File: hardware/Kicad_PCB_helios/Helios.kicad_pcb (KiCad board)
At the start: 2 copper layers, 75.2 x 61.1 mm, 101 parts, among them P1 USB_B, P2 CONN_01X25-SHIELD, U1 IP4220CZ6, U2 AP2114, U3 AN431B, U4 ISA_DC-DC_converter, U5 DAC084S085C, U6 TL084_v, U7 LM358, U8 TL084_v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

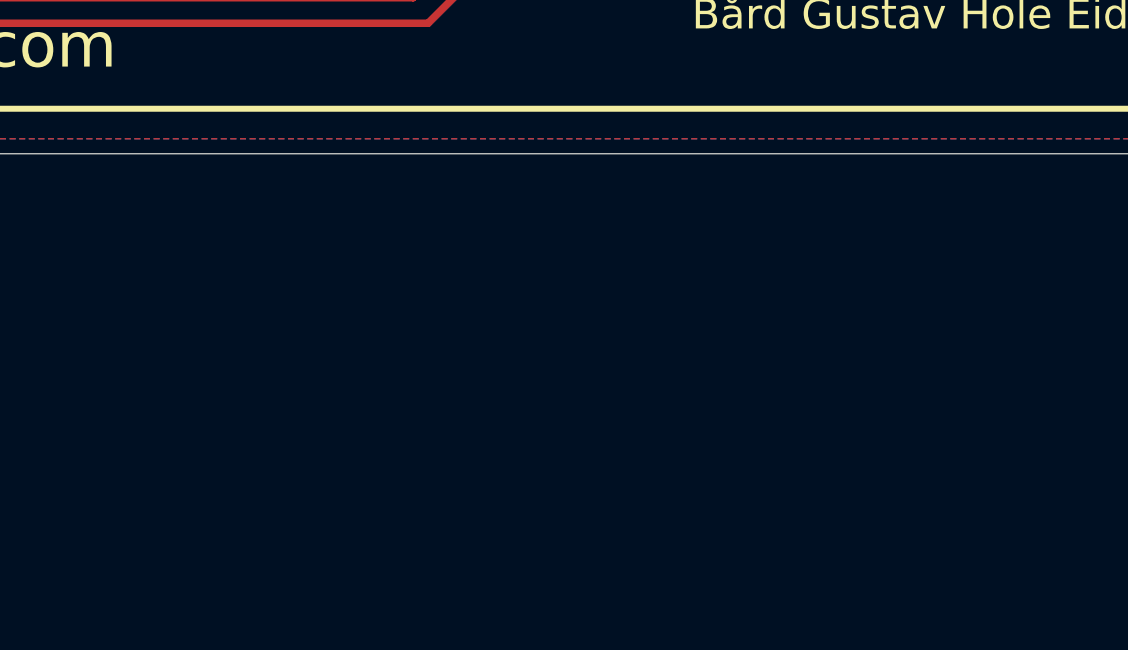
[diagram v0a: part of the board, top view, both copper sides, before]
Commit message: Dodano 2 zewnętrzne 16 bitowe układy DAC
Podłączono VREF do wewnętrznych DAC

Wszystko działa na jednej magistrali SPI
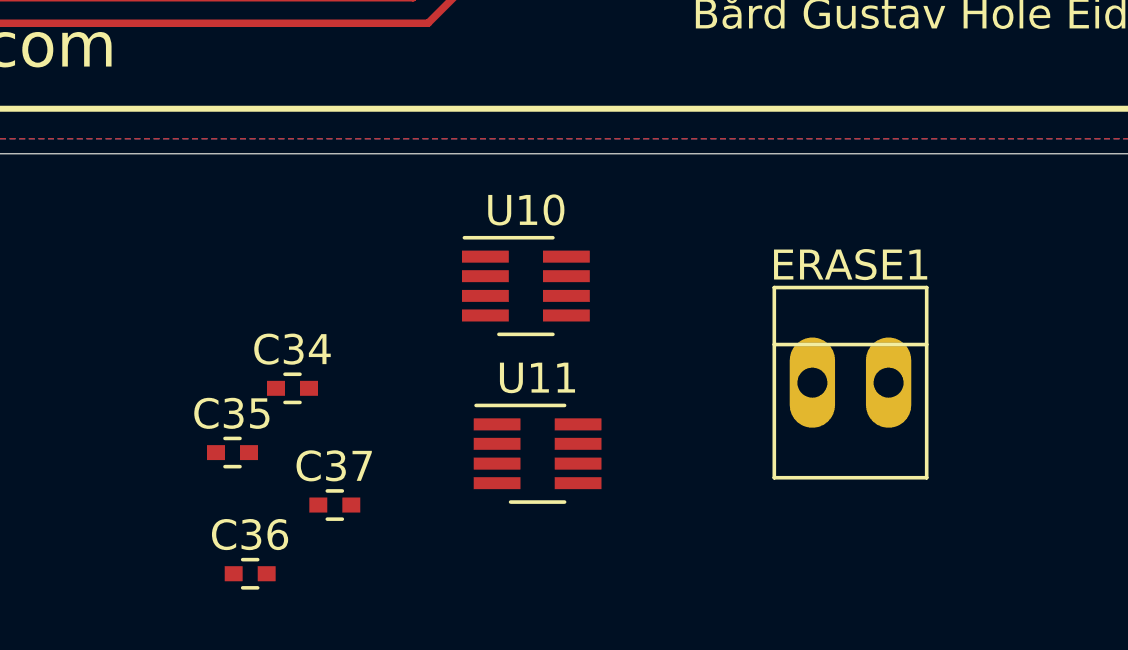
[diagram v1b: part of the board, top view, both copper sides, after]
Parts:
- added C34: 100nF, Capacitors_SMD:C_0402, F.Cu at (129.4, 168.9)
- added C35: 100nF, Capacitors_SMD:C_0402, F.Cu at (127.4, 171.1)
- added C36: 10nF, Capacitors_SMD:C_0402, F.Cu at (128.0, 175.1)
- added C37: 10nF, Capacitors_SMD:C_0402, F.Cu at (130.8, 172.8)
- added ERASE1: CONN_01X02, Connect:PINHEAD1-2, F.Cu at (146.8, 168.7)
- added U10: DAC8531, TO_SOT_Packages_SMD:SOT-23-8_Handsoldering, F.Cu at (137.2, 165.5)
- added U11: DAC8531, TO_SOT_Packages_SMD:SOT-23-8_Handsoldering, F.Cu at (137.6, 171.1)
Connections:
- net /Amplifiers/+9V renamed /+9V
- net /Amplifiers/+B renamed /+B
- net /Amplifiers/+G renamed /+G
- net /Amplifiers/+Intensity renamed /+Int
- net /Amplifiers/+R renamed /+R
- net /Amplifiers/+X renamed /+X
- net /Amplifiers/+Y renamed /+Y
- net /Amplifiers/-9V renamed /-9V
- net /Amplifiers/-X renamed /-X
- net /Amplifiers/-Y renamed /-Y
- net /Amplifiers/2.5V renamed /2.5V
- net /Amplifiers/B renamed /B
- net /Amplifiers/G renamed /G
- net /Amplifiers/Intensity renamed /Int
- net /Amplifiers/R renamed /R
- net /Amplifiers/Shutter renamed /Shutter
- net /Amplifiers/Shutter_Out renamed /Shutter_Out
- net /DAC/!SYNC renamed /DAC/!SYNC-Quad
- net /Power Regulation/5V renamed /VCC
- C10 pad 1: /DAC/3.3V -> /3.3V
- C11 pad 1: /DAC/3.3V -> /3.3V
- C21 pad 1: /DAC/3.3V -> /3.3V
- C23 pad 1: /DAC/3.3V -> /3.3V
- C25 pad 1: /DAC/3.3V -> /3.3V
- C26 pad 1: /DAC/3.3V -> /3.3V
- C27 pad 1: /DAC/3.3V -> /3.3V
- ERASE pad 2: /DAC/3.3V -> (no net)
- F1 pad 1: Net-(F1-Pad1) -> Net-(C2-Pad1)
- P1 pad 1: Net-(F1-Pad1) -> Net-(C2-Pad1)
- P1 pad 5: Net-(C2-Pad1) -> GND
- R12 pad 1: /DAC/3.3V -> /3.3V
- R13 pad 1: /DAC/3.3V -> /3.3V
- R33 pad 1: Net-(R33-Pad1) -> (no net)
- R34 pad 1: Net-(R34-Pad1) -> (no net)
- U2 pad 2: /DAC/3.3V -> /3.3V
- U5 pad 1: /DAC/3.3V -> /3.3V
- U8 pad 10: Net-(R34-Pad1) -> /Amplifiers/Offset
- U8 pad 3: Net-(R33-Pad1) -> /Amplifiers/Offset
- U9 pad 18: /DAC/3.3V -> /3.3V
- U9 pad 29: (no net) -> /DAC/!SYNC-X
- U9 pad 30: (no net) -> /DAC/!SYNC-Y
- U9 pad 45: /DAC/3.3V -> /3.3V
- U9 pad 58: /DAC/3.3V -> /3.3V
- U9 pad 59: /Amplifiers/X -> /DAC/X_SCALING
- U9 pad 63: /Amplifiers/Y -> /DAC/Y_SCALING
- U9 pad 7: /DAC/3.3V -> /3.3V
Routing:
- net /DAC/3.3V: track 95.3 -> 0.00 mm, vias 2 -> 0
- net /3.3V: track 0.00 -> 95.3 mm, vias 0 -> 2
- net /DAC/Y_SCALING: track 0.00 -> 21.6 mm, vias 0 -> 2
- net /Amplifiers/Y: track 45.6 -> 24.0 mm, vias 4 -> 2
- net Net-(F1-Pad1): track 17.2 -> 0.00 mm
- net GND: track 138.7 -> 151.8 mm
- net /DAC/X_SCALING: track 0.00 -> 12.7 mm, vias 0 -> 1
- net /Amplifiers/X: track 44.5 -> 31.8 mm, vias 2 -> 1
- net /Amplifiers/Offset: track 17.3 -> 28.3 mm
- net Net-(R34-Pad1): track 6.09 -> 0.00 mm
- net Net-(R33-Pad1): track 4.89 -> 0.00 mm
- net Net-(C2-Pad1): track 15.5 -> 19.6 mm

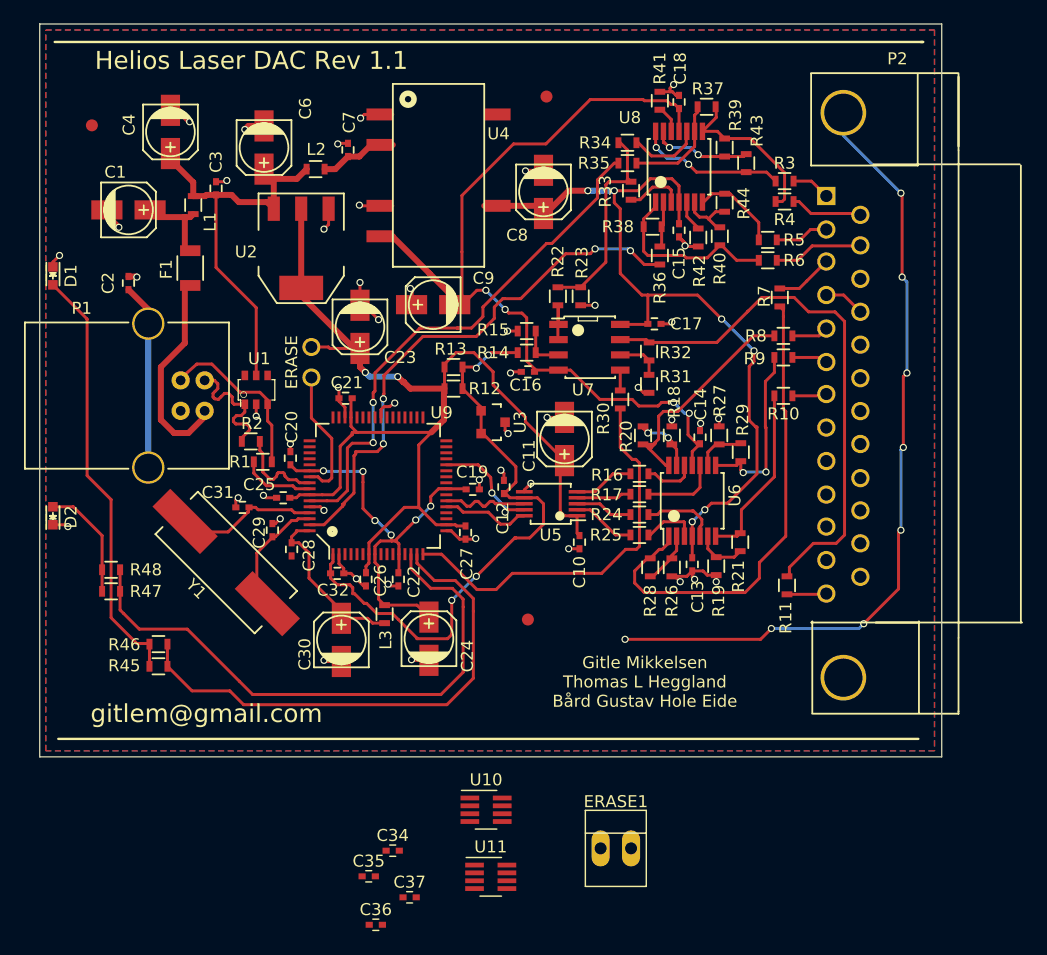
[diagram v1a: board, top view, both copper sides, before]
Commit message: Updated PCB Layout
Changed connector to IDC
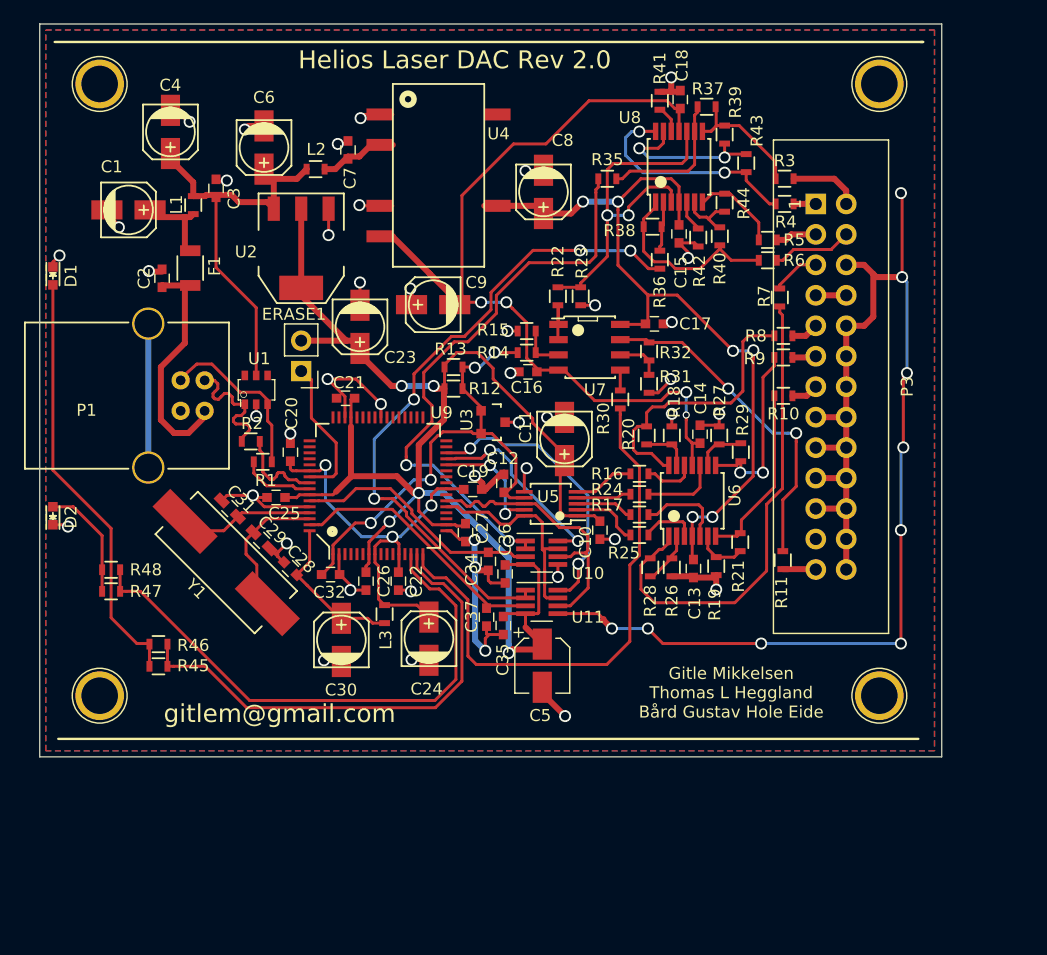
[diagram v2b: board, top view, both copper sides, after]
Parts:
- removed ERASE: CONN_01X02, Connect:PINHEAD1-2
- removed P2: CONN_01X25-SHIELD, personal:DB25
- removed R33, R34: 1.65k, Resistors_SMD:R_0603
- removed REF** (x3): Fiducial_1mm_Dia_2.54mm_Outer_CopperTop, Fiducials:Fiducial_1mm_Dia_2.54mm_Outer_CopperTop
- added C5: 4.7uF, Capacitors_SMD:CP_Elec_4x5.3, F.Cu at (141.9, 153.5)
- added P3: CONN_02X13, Connectors:IDC_Header_Straight_26pins, F.Cu at (164.7, 115.0)
- added W1: TEST_1P, Connectors:1pin, F.Cu at (105.0, 156.0)
- added W2: TEST_1P, Connectors:1pin, F.Cu at (105.0, 105.0)
- added W3: TEST_1P, Connectors:1pin, F.Cu at (170.0, 156.0)
- added W4: TEST_1P, Connectors:1pin, F.Cu at (170.0, 105.0)
- added W5: TEST_1P, Symbols:WEEE-Logo_14x20mm_SilkScreen, B.Cu at (149.7, 129.9)
- C10, C12, C13, C14, C15, C16, C17, C18, C19, C2, C20, C21, C22, C25, C26, C27, C28, C3, C32, C34, C35, C36, C37, C7: footprint Capacitors_SMD:C_0402 -> Capacitors_SMD:C_0603
- C29, C31: footprint Capacitors_SMD:C_0402 -> Capacitors_SMD:C_0603_HandSoldering
- ERASE1: footprint Connect:PINHEAD1-2 -> Pin_Headers:Pin_Header_Straight_1x02_Pitch2.54mm
- moved ERASE1 47.0 mm to (121.8, 128.9), turned to 180 degrees
- moved C36 31.7 mm to (137.4, 144.8), turned to 270 degrees
- moved C34 24.9 mm to (138.8, 145.8), turned to 270 degrees
- moved C37 24.2 mm to (137.2, 149.4), turned to 270 degrees
- moved C35 23.7 mm to (138.7, 150.2), turned to 270 degrees
- moved U11 23.3 mm to (141.8, 148.2)
- moved U10 21.9 mm to (141.8, 144.1)
- moved C2 2.83 mm to (110.2, 121.2)
- moved R11 2.13 mm to (161.9, 144.7)
- moved R35 2.13 mm to (147.3, 112.9)
- moved C10 1.97 mm to (146.7, 142.2)
- moved R3 1.90 mm to (162.1, 115.0)
- moved R4 1.90 mm to (162.1, 112.9)
- moved C28 1.60 mm to (120.9, 145.4), turned to 135 degrees
- moved C29 1.24 mm to (118.5, 143.1), turned to 315 degrees
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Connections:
- R10 pad 1: Net-(P2-Pad7) -> /X7
- R11 pad 1: Net-(P2-Pad13) -> /X13
- R3 pad 1: Net-(P2-Pad1) -> /X1
- R4 pad 1: Net-(P2-Pad14) -> /X14
- R5 pad 1: Net-(P2-Pad2) -> /X2
- R6 pad 1: Net-(P2-Pad15) -> /X15
- R7 pad 1: Net-(P2-Pad3) -> /X3
- R8 pad 1: Net-(P2-Pad5) -> /X5
- R9 pad 1: Net-(P2-Pad6) -> /X6
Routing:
- net GND: track 151.8 -> 234.1 mm, vias 55 -> 53
- net /3.3V: track 95.3 -> 129.7 mm, vias 2 -> 5
- net /Amplifiers/Y: track 24.0 -> 55.0 mm, vias 2 -> 5
- net /DAC/!SYNC-Y: track 0.00 -> 23.8 mm, vias 0 -> 2
- net /Shutter_Out: track 45.7 -> 28.2 mm, vias 0 -> 2
- net /DAC/!SYNC-X: track 0.00 -> 16.7 mm, vias 0 -> 2
- net /DAC/Din: track 7.27 -> 23.7 mm
- net /Amplifiers/X: track 31.8 -> 47.9 mm, vias 1 -> 2
- net /Shutter: track 33.1 -> 45.6 mm
- net /DAC/SCLK: track 7.79 -> 18.2 mm
- net /2.5V: track 51.6 -> 41.6 mm
- net /DAC/X_SCALING: track 12.7 -> 20.9 mm, vias 1 -> 0
- net Net-(P2-Pad15): track 7.49 -> 0.00 mm
- net /X15: track 0.00 -> 6.70 mm
- net /+X: track 12.5 -> 18.8 mm
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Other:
- board text added: "Helios Laser DAC Rev 2.0"
- board text removed: "Helios Laser DAC Rev 1.1"
